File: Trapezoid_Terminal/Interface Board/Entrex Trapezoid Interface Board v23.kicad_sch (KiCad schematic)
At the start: 103 parts, among them P15 Conn_02x40_Odd_Even_Shielded, SW1 SW_DIP_x08

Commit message: Updated schematics during tutorial
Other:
- note added: "Terminal Back I/O Plug "CG1""
- note removed: "Terminal Back I/O Plug"
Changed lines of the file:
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@@
     (stroke (width 0) (type default))
   )
+  (bus (pts (xy 97.155 212.725) (xy 97.155 213.995))
+    (stroke (width 0) (type default))
+  )
   (wire (pts (xy 455.93 422.91) (xy 455.93 562.61))
     (stroke (width 0) (type default))
@@
     )
   )
-  (text_box "Duplex Switch DPDT\nCG1 or CG2\n"
+  (text_box "Duplex Switch DPDT with CENTER OFF\nCG1 or CG2\n"
     (at 104.775 118.745 0) (size 40.005 41.91)
     (stroke (width 0) (type default))
@@
     (effects (font (size 3 3) (thickness 1) bold (color 5 102 8 1)) (justify right bottom))
   )
+  (text "*" (at 170.18 196.215 0)
+    (effects (font (size 3 3) (thickness 1) bold (color 18 244 255 1)) (justify left bottom))
+  )
   (text "*" (at 181.61 864.87 0)
     (effects (font (size 3 3) (thickness 1) bold (color 255 38 190 1)) (justify right bottom))
@@
     (effects (font (size 3 3) (thickness 1) bold (color 18 244 255 1)) (justify left bottom))
   )
-  (text "Terminal Back \n   I/O Plug\n" (at 96.52 201.93 0)
+  (text "Terminal Back \nI/O Plug \"CG1\"\n" (at 92.71 202.565 0)
     (effects (font (size 5 5) (thickness 1) bold) (justify left bottom))
   )
@@
     (effects (font (size 3 3) (thickness 1) bold (color 5 102 8 1)) (justify right bottom))
   )
+  (text "*" (at 170.18 199.39 0)
+    (effects (font (size 3 3) (thickness 1) bold (color 18 244 255 1)) (justify left bottom))
+  )
   (text "*" (at 750.57 161.925 0)
     (effects (font (size 3 3) (thickness 1) bold (color 5 102 8 1)) (justify right bottom))
@@
     (effects (font (size 3 3) (thickness 1) bold (color 18 244 255 1)) (justify left bottom))
   )
+  (text "*" (at 170.18 189.865 0)
+    (effects (font (size 3 3) (thickness 1) bold (color 18 244 255 1)) (justify left bottom))
+  )
   (text "*" (at 169.545 290.195 0)
     (effects (font (size 3 3) (thickness 1) bold (color 18 244 255 1)) (justify left bottom))
@@
     (effects (font (size 3 3) (thickness 1) bold (color 5 102 8 1)) (justify right bottom))
   )
+  (text "*" (at 170.18 180.34 0)
+    (effects (font (size 3 3) (thickness 1) bold (color 18 244 255 1)) (justify left bottom))
+  )
   (text "*" (at 647.065 320.675 0)
     (effects (font (size 3 3) (thickness 1) bold (color 5 102 8 1)) (justify right bottom))
@@
     (effects (font (size 3 3) (thickness 1) bold (color 0 0 132 1)) (justify right bottom))
   )
+  (text "*" (at 170.18 193.04 0)
+    (effects (font (size 3 3) (thickness 1) bold (color 18 244 255 1)) (justify left bottom))
+  )
   (text "*" (at 246.38 161.925 0)
     (effects (font (size 3 3) (thickness 1) bold (color 18 244 255 1)) (justify left bottom))
@@
     (effects (font (size 3 3) (thickness 1) bold (color 5 102 8 1)) (justify right bottom))
   )
+  (text "*" (at 170.18 183.515 0)
+    (effects (font (size 3 3) (thickness 1) bold (color 18 244 255 1)) (justify left bottom))
+  )
   (text "*" (at 974.09 368.3 0)
     (effects (font (size 3 3) (thickness 1) bold (color 0 0 132 1)) (justify right bottom))
@@
     (effects (font (size 3 3) (thickness 1) bold (color 5 102 8 1)) (justify right bottom))
   )
-  (text "*" (at 139.7 201.93 0)
-    (effects (font (size 3 3) (thickness 1) bold (color 18 244 255 1)) (justify left bottom))
-  )
   (text "x" (at 26.67 66.675 0)
     (effects (font (size 3 3) (thickness 1) bold (color 255 30 30 1)) (justify right bottom))
@@
     (effects (font (size 3 3) (thickness 1) bold (color 255 38 190 1)) (justify right bottom))
   )
+  (text "*" (at 170.18 201.93 0)
+    (effects (font (size 3 3) (thickness 1) bold (color 18 244 255 1)) (justify left bottom))
+  )
   (text "*" (at 865.505 450.85 0)
     (effects (font (size 3 3) (thickness 1) bold (color 255 38 190 1)) (justify right bottom))
@@
     (effects (font (size 3 3) (thickness 1) bold (color 5 102 8 1)) (justify right bottom))
   )
+  (text "*" (at 146.05 194.945 0)
+    (effects (font (size 3 3) (thickness 1) bold (color 18 244 255 1)) (justify left bottom))
+  )
+  (text "*" (at 170.18 186.69 0)
+    (effects (font (size 3 3) (thickness 1) bold (color 18 244 255 1)) (justify left bottom))
+  )
   (text "*" (at 149.86 229.235 0)
     (effects (font (size 3 3) (thickness 1) bold (color 18 244 255 1)) (justify left bottom))
@@
     (effects (font (size 1.27 1.27)) (justify left bottom))
   )
+  (label "{P15_37 P15_38 P15_39 P15_40 P15_41 P15_42 P15_43 P15_44 P15_45 P15_46}"
+    (at 97.155 213.36 0) (fields_autoplaced)
+    (effects (font (size 0.25 0.25)) (justify left bottom))
+  )
   (label "VCC" (at 1192.53 718.185 90) (fields_autoplaced)

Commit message: fix interface board errors
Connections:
- net XX(UA3P5) is gone; now on net VCC: UA3.5 (D10)
- net XX(UA4P5) is gone; now on net VCC: UA4.5 (D10)
- net XX(UE5P9) is gone; now on net u4_2: UE5.9 (CC)
- net u4_3 is gone; now on net u16_15: R17.1, UA7.9, UD8.3, UE7.10
- net u4_2: now also UE6.13 (2STRB)
- no-connect marks 98 -> 94
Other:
- note added: "Data Trans"
- note added: "Input 1"
- note added: "Input 2"
- note added: "Input 3"
- note added: "Other Trans"
- moved on the sheet: C24

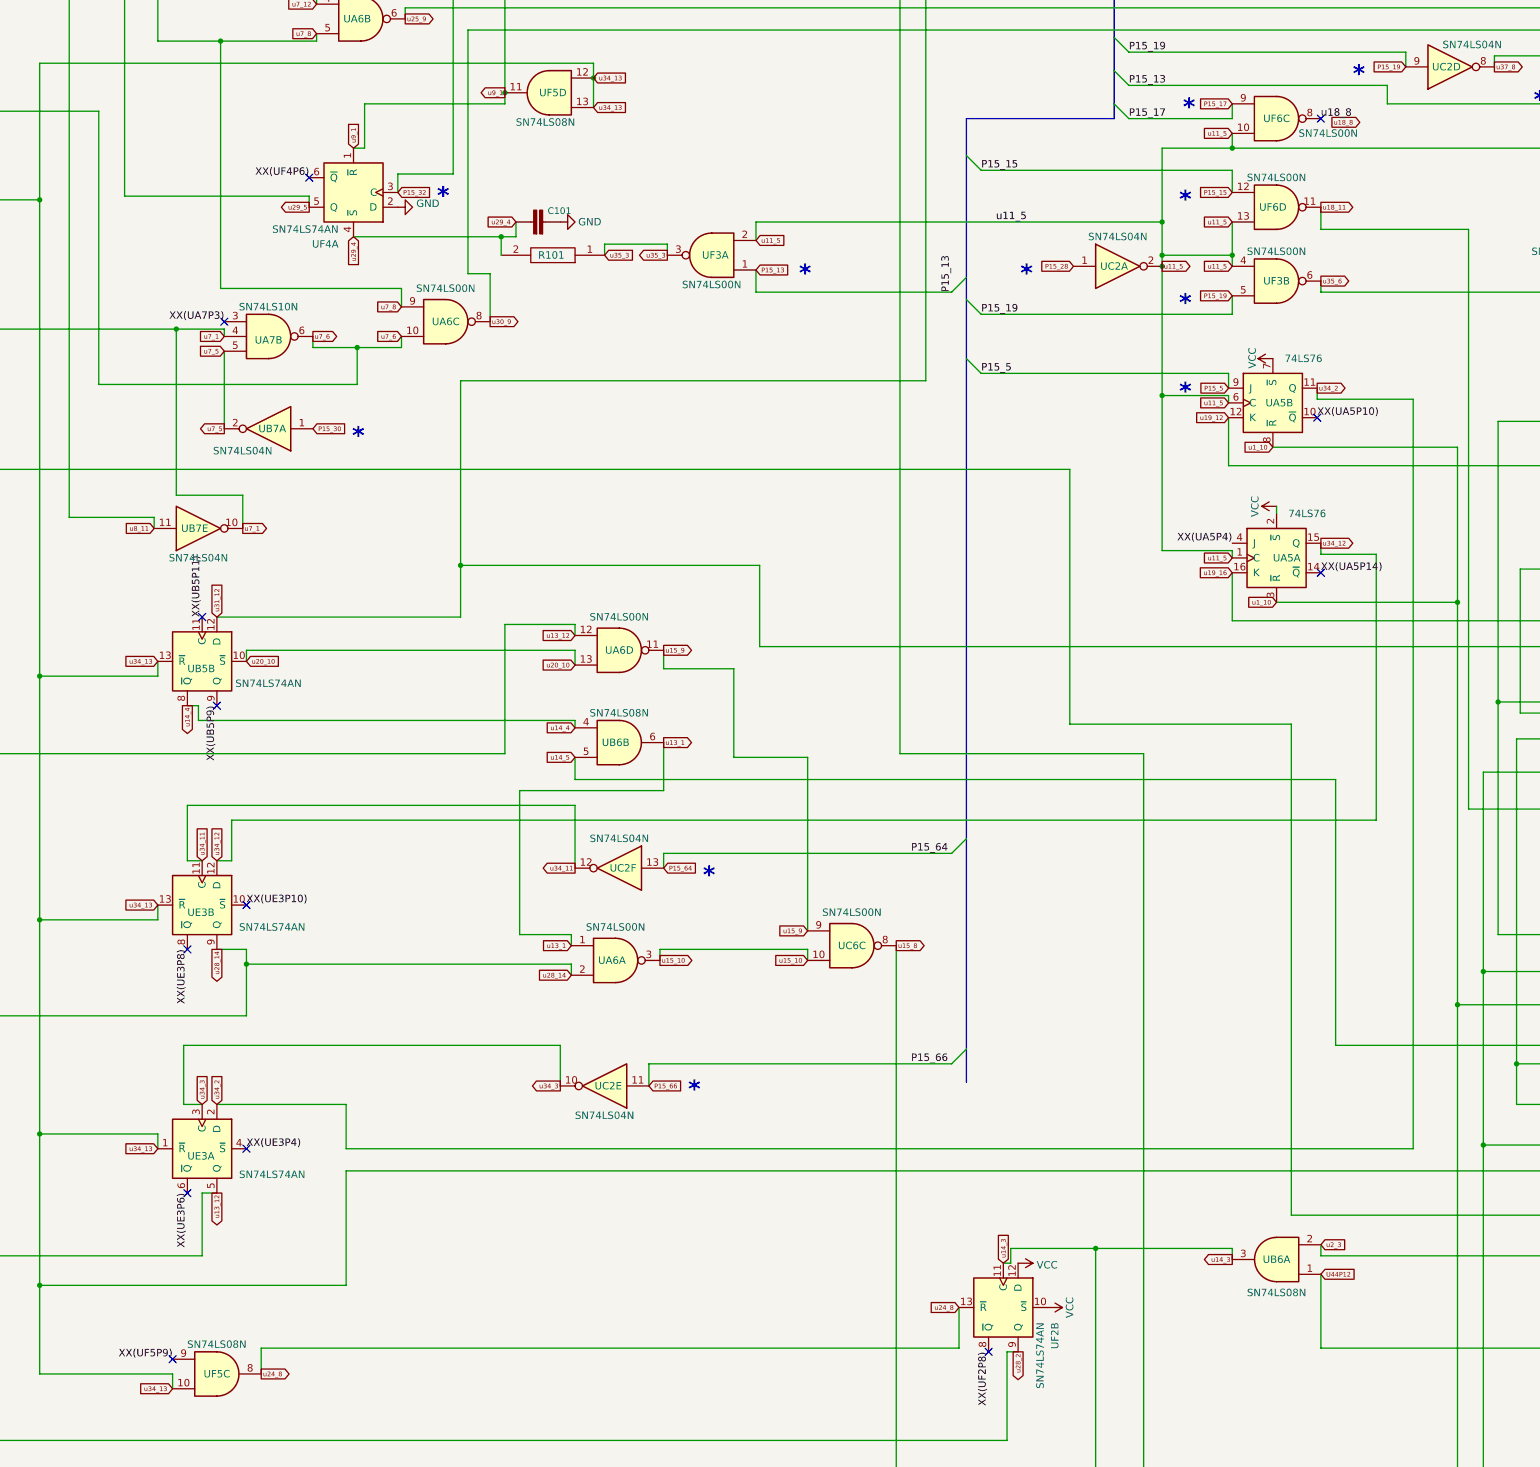
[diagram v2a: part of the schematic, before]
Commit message: UF5 pin 9 connection
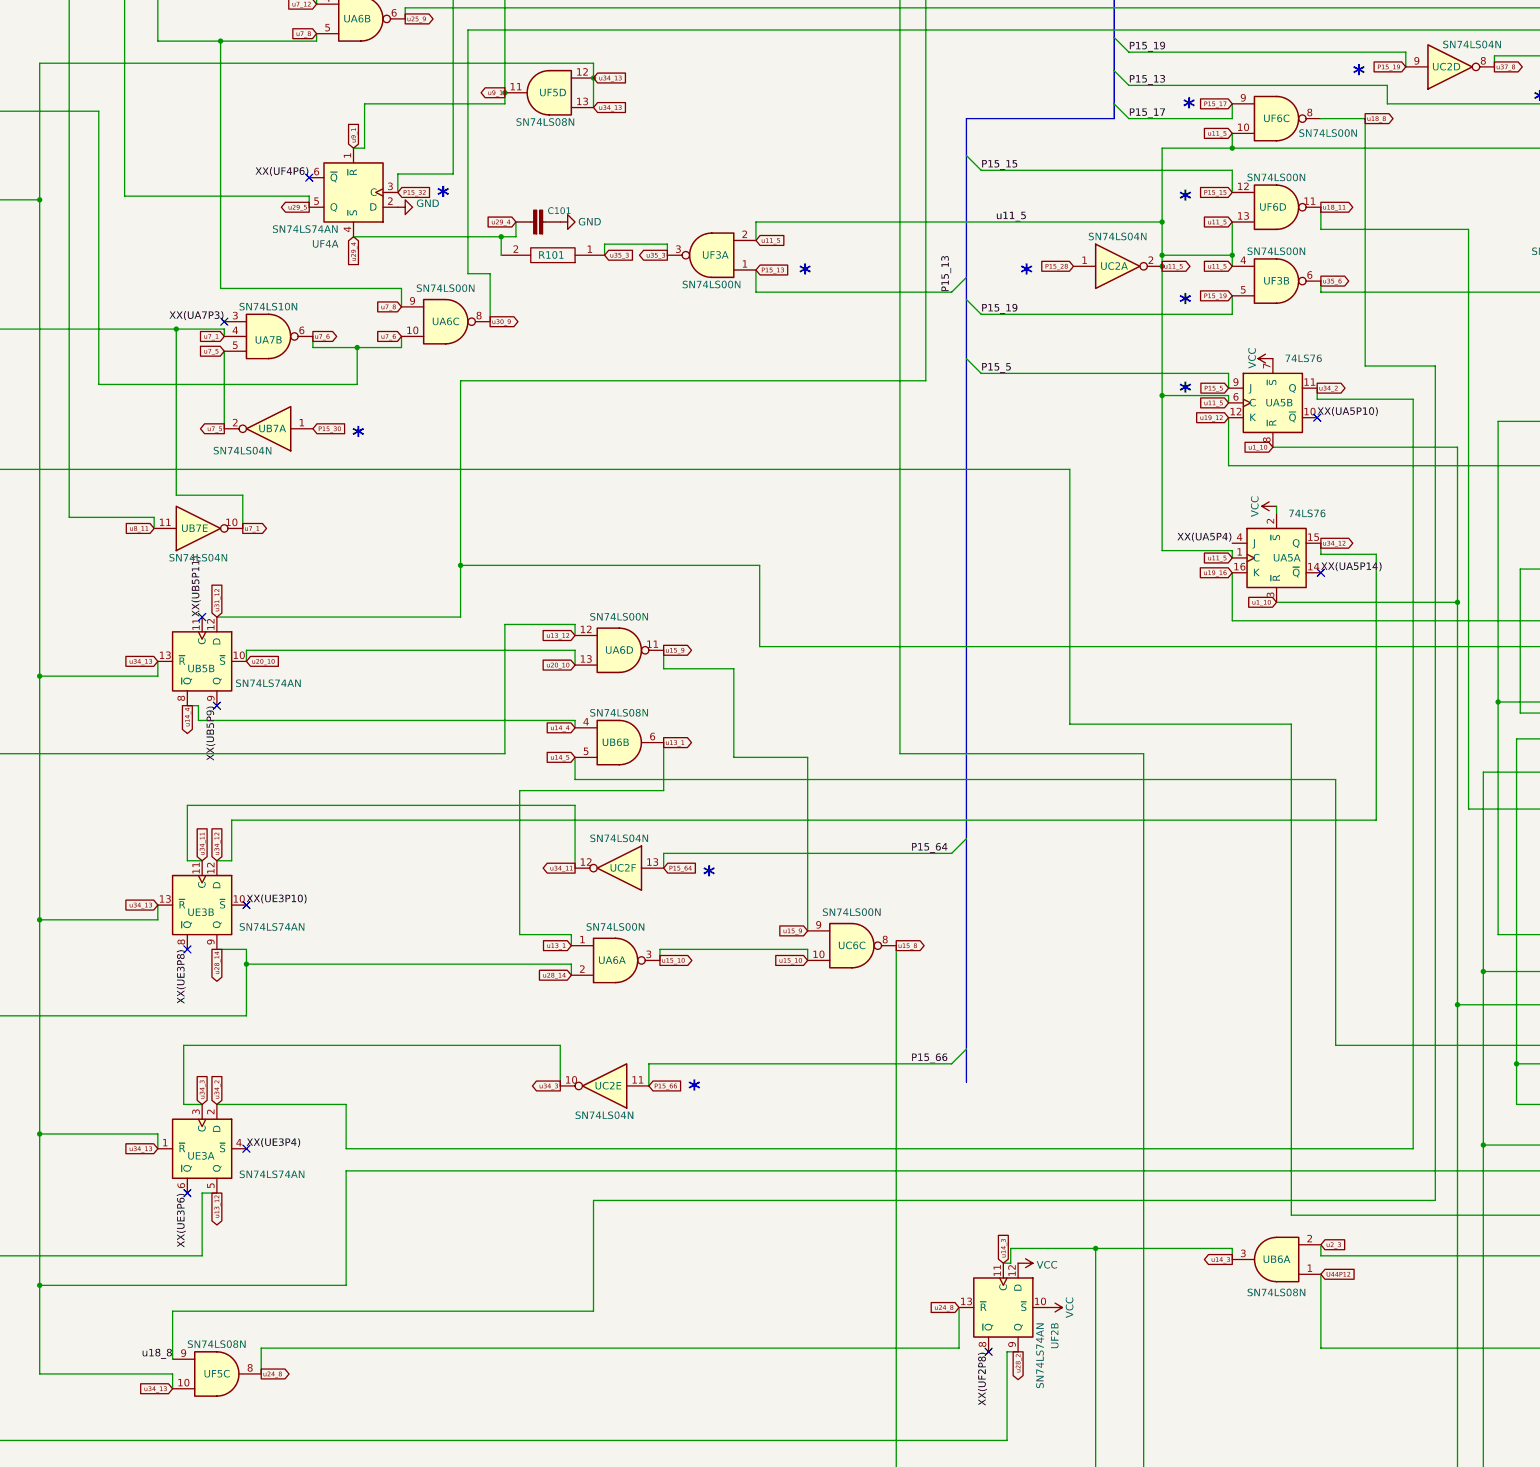
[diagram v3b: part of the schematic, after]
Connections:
- net XX(UF5P9) is gone; now on net u18_8: UF5.9
- no-connect marks 94 -> 92
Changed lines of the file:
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@@
   (no_connect (at 528.32 531.495))
   (no_connect (at 407.67 204.47))
-  (no_connect (at 330.835 666.75))
   (no_connect (at 261.62 462.28))
   (no_connect (at 354.33 463.55))
@@
   (no_connect (at 120.396 79.375))
   (no_connect (at 739.775 249.555))
-  (no_connect (at 528.32 453.39))
   (no_connect (at 285.75 187.325))
   (no_connect (at 143.51 234.315))
@@
     (stroke (width 0) (type default))
   )
+  (wire (pts (xy 548.005 495.935) (xy 548.005 639.445))
+    (stroke (width 0) (type default))
+  )
   (wire (pts (xy 702.945 297.18) (xy 702.945 318.77))
     (stroke (width 0) (type default))
@@
     (stroke (width 0) (type default))
   )
+  (wire (pts (xy 535.94 453.39) (xy 535.94 495.935))
+    (stroke (width 0) (type default))
+  )
   (wire (pts (xy 106.68 82.55) (xy 160.02 82.55))
     (stroke (width 0) (type default))
@@
     (stroke (width 0) (type default))
   )
+  (wire (pts (xy 535.94 495.935) (xy 548.005 495.935))
+    (stroke (width 0) (type default))
+  )
   (wire (pts (xy 575.31 530.86) (xy 575.31 527.05))
     (stroke (width 0) (type default))
@@
     (stroke (width 0) (type default))
   )
+  (wire (pts (xy 330.835 658.495) (xy 403.225 658.495))
+    (stroke (width 0) (type default))
+  )
   (wire (pts (xy 653.415 715.01) (xy 653.415 721.36))
     (stroke (width 0) (type default))
@@
     (stroke (width 0) (type default))
   )
+  (wire (pts (xy 330.835 666.75) (xy 330.835 658.495))
+    (stroke (width 0) (type default))
+  )
   (wire (pts (xy 495.3 441.96) (xy 542.925 441.96))
     (stroke (width 0) (type default))
@@
     (stroke (width 0) (type default))
   )
+  (wire (pts (xy 403.225 658.495) (xy 403.225 639.445))
+    (stroke (width 0) (type default))
+  )
   (wire (pts (xy 544.83 290.195) (xy 685.165 290.195))
     (stroke (width 0) (type default))
@@
     (stroke (width 0) (type default))
   )
+  (wire (pts (xy 528.32 453.39) (xy 535.94 453.39))
+    (stroke (width 0) (type default))
+  )
   (wire (pts (xy 575.945 648.97) (xy 528.32 648.97))
     (stroke (width 0) (type default))
@@
     (stroke (width 0) (type default))
   )
+  (wire (pts (xy 403.225 639.445) (xy 548.005 639.445))
+    (stroke (width 0) (type default))
+  )
   (wire (pts (xy 206.375 795.655) (xy 211.455 795.655))
     (stroke (width 0) (type default))
@@
     (effects (font (size 1.27 1.27)) (justify right bottom))
   )
-  (label "u4_2" (at 255.27 198.755 180)
+  (label "u4_2" (at 255.27 198.755 180) (fields_autoplaced)
     (effects (font (size 1.27 1.27)) (justify right bottom))
   )
@@
     (effects (font (size 1.27 1.27)) (justify right bottom))
   )
-  (label "XX(UF5P9)" (at 330.835 666.75 180) (fields_autoplaced)
+  (label "u18_8" (at 330.835 666.75 180) (fields_autoplaced)
     (effects (font (size 1.27 1.27)) (justify right bottom))
   )
@@
     (effects (font (size 1.27 1.27)) (justify right bottom))
   )
-  (label "u18_8" (at 528.32 453.39 0) (fields_autoplaced)
-    (effects (font (size 1.27 1.27)) (justify left bottom))
-  )
   (label "XX(UD7P2)" (at 408.305 178.435 180) (fields_autoplaced)
     (effects (font (size 1.27 1.27)) (justify right bottom))
@@
     )
   )
-  (global_label "u18_8" (shape output) (at 530.225 454.025 0) (fields_autoplaced)
+  (global_label "u18_8" (shape output) (at 535.94 453.39 0) (fields_autoplaced)
     (effects (font (size 0.8 0.8)) (justify left))
-    (property "Intersheetrefs" "${INTERSHEET_REFS}" (at 535.6743 454.025 0)
+    (property "Intersheetrefs" "${INTERSHEET_REFS}" (at 541.3893 453.39 0)
       (effects (font (size 0.8 0.8)) (justify left) hide)
     )
